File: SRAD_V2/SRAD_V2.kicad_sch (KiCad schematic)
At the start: 39 parts, among them SW1 SW_Push_Dual, SW2 SW_Nidec_CAS-120A1, U1 STM32F767ZIT6, U12 MAX-M10S, U13 MS5607-02BA, U14 MMC5983MA, U17 AS5F31G04SND-08LIN, U4 LSM6DSV80XTR

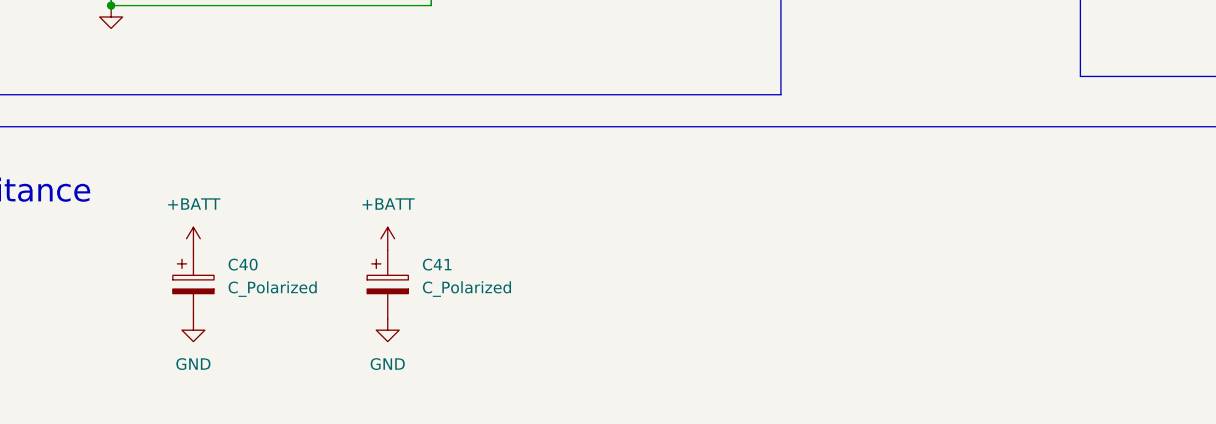
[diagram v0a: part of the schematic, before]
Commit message: Added an input LC filter
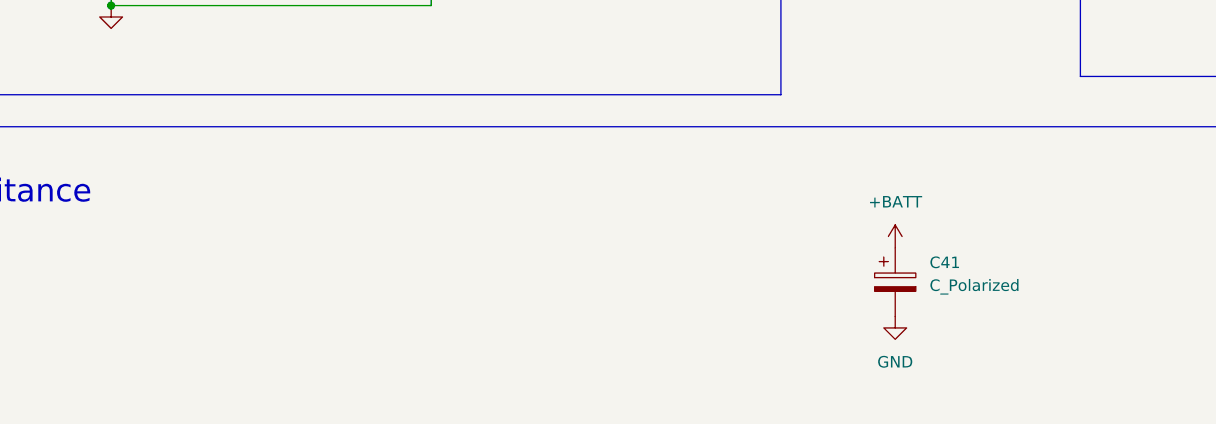
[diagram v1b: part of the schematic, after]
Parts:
- removed C40: C_Polarized, symbol Device:C_Polarized
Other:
- moved on the sheet: C41

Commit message: fiddling with the layout
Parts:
- removed SW1: SW_Push_Dual, Button_Switch_SMD:SW_DIP_SPSTx02_Slide_6.7x6.64mm_W6.73mm_P2.54mm_LowProfile_JPin, symbol Switch:SW_Push_Dual
- removed SW2: SW_Nidec_CAS-120A1, Button_Switch_SMD:Nidec_Copal_CAS-120A, symbol Switch:SW_Nidec_CAS-120A1
- added D1: WL-SMCW_1206, 150120SS75000:WL-SMCW_1206, symbol Red Led:WL-SMCW_1206
- added R13: 1k, symbol Device:R_Small
- added S1: TS18-5-15-SL-160-SMT-TR, push_button:SW_TS18-5-15-SL-160-SMT-TR, symbol push_button:TS18-5-15-SL-160-SMT-TR
- added S2: SLW-913535-2A-SMT, spdt_switch:SW_SLW-913535-2A-SMT, symbol spdt_switch:SLW-913535-2A-SMT
- FB1: footprint (none) -> Inductor_SMD:L_0603_1608Metric
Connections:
- net +3.3V: now also D1.2, S2.1, S2.4
- net GND: now also R13.2, S1.3, S1.4, S2.3, S2.6
- net at C39.2, U1.25 (NRST): now also S1.1, S1.2
- net at U1.138 (BOOT0): now also S2.2, S2.5
- new net: D1.1, R13.1
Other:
- note added: "LED indicator"
- note added: "approx 1.4mA of current"
- note added: "input capacitance"
- note removed: "Bulk Capacitance"
- moved on the sheet: C41

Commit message: more routing
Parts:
- R13: footprint (none) -> Resistor_SMD:R_0603_1608Metric
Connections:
- net +3.3V: now also C10.1, C11.1, C16.2, C17.2, C18.2, C20.2, C21.2, C22.2, C23.1, C24.2, U12.7 (VCC_IO), U12.8 (VCC), U13.1 (VDD), U14.13 (VDDIO), U14.2 (VDD), U17.8 (VCC), U4.5 (VDDIO), U4.8 (VDD)
- removed net +3V3: C10.1, C11.1, C16.2, C17.2, C18.2, C20.2, C21.2, C22.2, C23.1, C24.2, U12.6 (V_BCKP), U12.7 (VCC_IO), U12.8 (VCC), U13.1 (VDD), U14.13 (VDDIO), U14.2 (VDD), U17.8 (VCC), U4.5 (VDDIO), U4.8 (VDD)
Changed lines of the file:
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@@
 	)
 	(junction
-		(at 193.04 193.04)
-		(diameter 0)
-		(color 0 0 0 0)
-	)
-	(junction
 		(at 177.8 106.68)
 		(diameter 0)
@@
 	)
 	(junction
+		(at 191.77 193.04)
+		(diameter 0)
+		(color 0 0 0 0)
+	)
+	(junction
 		(at 95.25 44.45)
 		(diameter 0)
@@
 	)
 	(junction
-		(at 193.04 196.85)
-		(diameter 0)
-		(color 0 0 0 0)
-	)
-	(junction
 		(at 300.228 35.56)
 		(diameter 0)
@@
 	(wire
 		(pts
-			(xy 191.77 196.85) (xy 193.04 196.85)
-		)
-		(stroke
-			(width 0)
-			(type default)
-		)
-	)
-	(wire
-		(pts
 			(xy 168.91 106.68) (xy 168.91 110.49)
 		)
@@
 	(wire
 		(pts
-			(xy 193.04 193.04) (xy 193.04 196.85)
-		)
-		(stroke
-			(width 0)
-			(type default)
-		)
-	)
-	(wire
-		(pts
 			(xy 177.8 160.02) (xy 180.34 160.02)
 		)
@@
 	(wire
 		(pts
-			(xy 229.87 193.04) (xy 193.04 193.04)
-		)
-		(stroke
-			(width 0)
-			(type default)
-		)
-	)
-	(wire
-		(pts
 			(xy 92.71 81.28) (xy 95.25 81.28)
 		)
@@
 	(wire
 		(pts
-			(xy 193.04 196.85) (xy 194.31 196.85)
+			(xy 27.94 76.2) (xy 29.21 76.2)
 		)
 		(stroke
@@
 	(wire
 		(pts
-			(xy 27.94 76.2) (xy 29.21 76.2)
+			(xy 121.92 73.66) (xy 129.54 73.66)
 		)
 		(stroke
@@
 	(wire
 		(pts
-			(xy 121.92 73.66) (xy 129.54 73.66)
+			(xy 191.77 193.04) (xy 191.77 196.85)
 		)
 		(stroke
@@
 	(wire
 		(pts
+			(xy 191.77 193.04) (xy 229.87 193.04)
+		)
+		(stroke
+			(width 0)
+			(type default)
+		)
+	)
+	(wire
+		(pts
 			(xy 297.434 35.56) (xy 300.228 35.56)
 		)
@@
 	(wire
 		(pts
-			(xy 193.04 193.04) (xy 189.23 193.04)
+			(xy 189.23 193.04) (xy 191.77 193.04)
 		)
 		(stroke
@@
 		)
 	)
-	(global_label "+3V3"
+	(global_label "+3.3V"
 		(shape input)
 		(at 386.08 96.52 0)
@@
 		)
 	)
-	(global_label "+3V3"
+	(global_label "+3.3V"
 		(shape input)
 		(at 381 210.82 0)
@@
 		)
 	)
-	(global_label "+3V3"
+	(global_label "+3.3V"
 		(shape input)
 		(at 177.8 160.02 180)
@@
 		)
 	)
-	(global_label "+3V3"
+	(global_label "+3.3V"
 		(shape input)
 		(at 233.68 165.1 0)
@@
 		)
 	)
-	(global_label "+3V3"
+	(global_label "+3.3V"
 		(shape input)
 		(at 246.38 110.49 0)
@@
 		)
 	)
-	(global_label "+3V3"
+	(global_label "+3.3V"
 		(shape input)
 		(at 165.1 106.68 180)
@@
 		)
 	)
-	(global_label "+3V3"
+	(global_label "+3.3V"
 		(shape input)
 		(at 186.69 193.04 180)
@@
 			)
 		)
-		(property "Footprint" ""
+		(property "Footprint" "Resistor_SMD:R_0603_1608Metric"
 			(at 206.756 266.446 0)
 			(hide yes)

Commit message: more layout optimisation
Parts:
- removed C41: C_Polarized, symbol Device:C_Polarized
- added J1: Conn_01x04_Pin, Connector_PinHeader_2.54mm:PinHeader_1x04_P2.54mm_Vertical, symbol Connector:Conn_01x04_Pin
- added J7: 691210910002, Screw_Terminal:691210910002, symbol Screw Terminal:691210910002
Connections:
- net +3.3V: now also J1.3 (Pin_3)
- net EM_CH1: now also U1.91 (PG6); no longer U1.105 (PA13)
- net EM_CH2: now also U1.90 (PG5); no longer U1.104 (PA12)
- net EM_CH3: now also U1.89 (PG4); no longer U1.103 (PA11)
- net EM_CH4: now also U1.88 (PG3); no longer U1.102 (PA10)
- net GND: now also J1.4 (Pin_4), J7.2
- net Buzzer: now reaches BZ2.1 (+)
- net Buzzer: now also U1.70 (PB11)
- net SWCLK: now reaches U1.109 (PA14)
- net SWCLK: now also J1.2 (Pin_2)
- new net +7.4VBATT: J7.1
- new net SWDIO: J1.1 (Pin_1), U1.105 (PA13)
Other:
- note removed: "input capacitance"
- moved on the sheet: S2

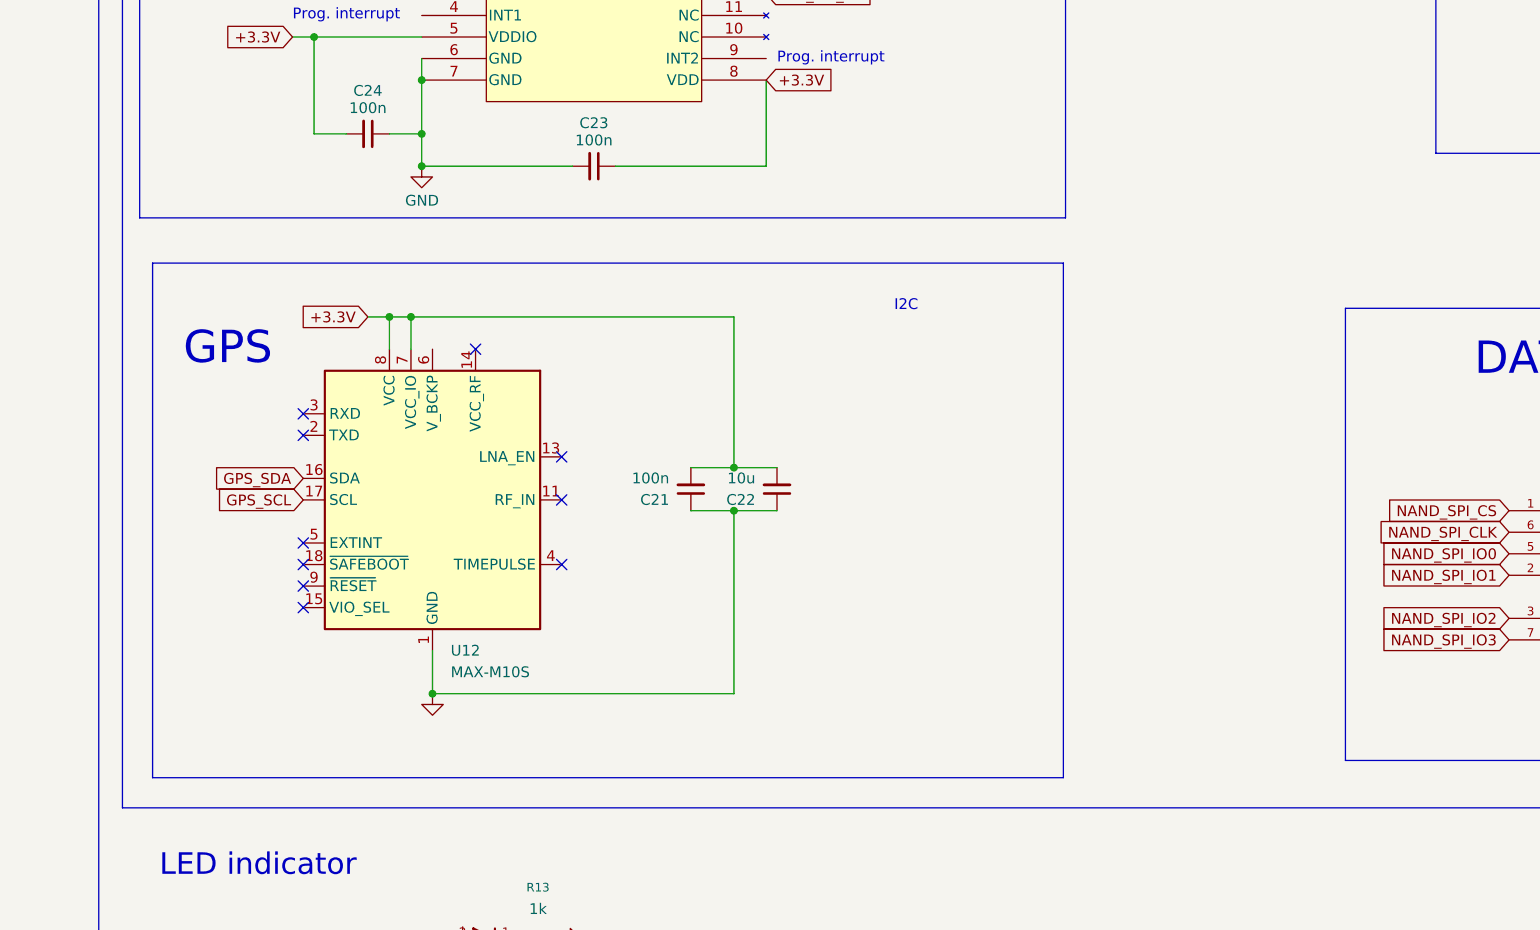
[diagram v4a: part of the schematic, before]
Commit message: Added important GPS circuitry
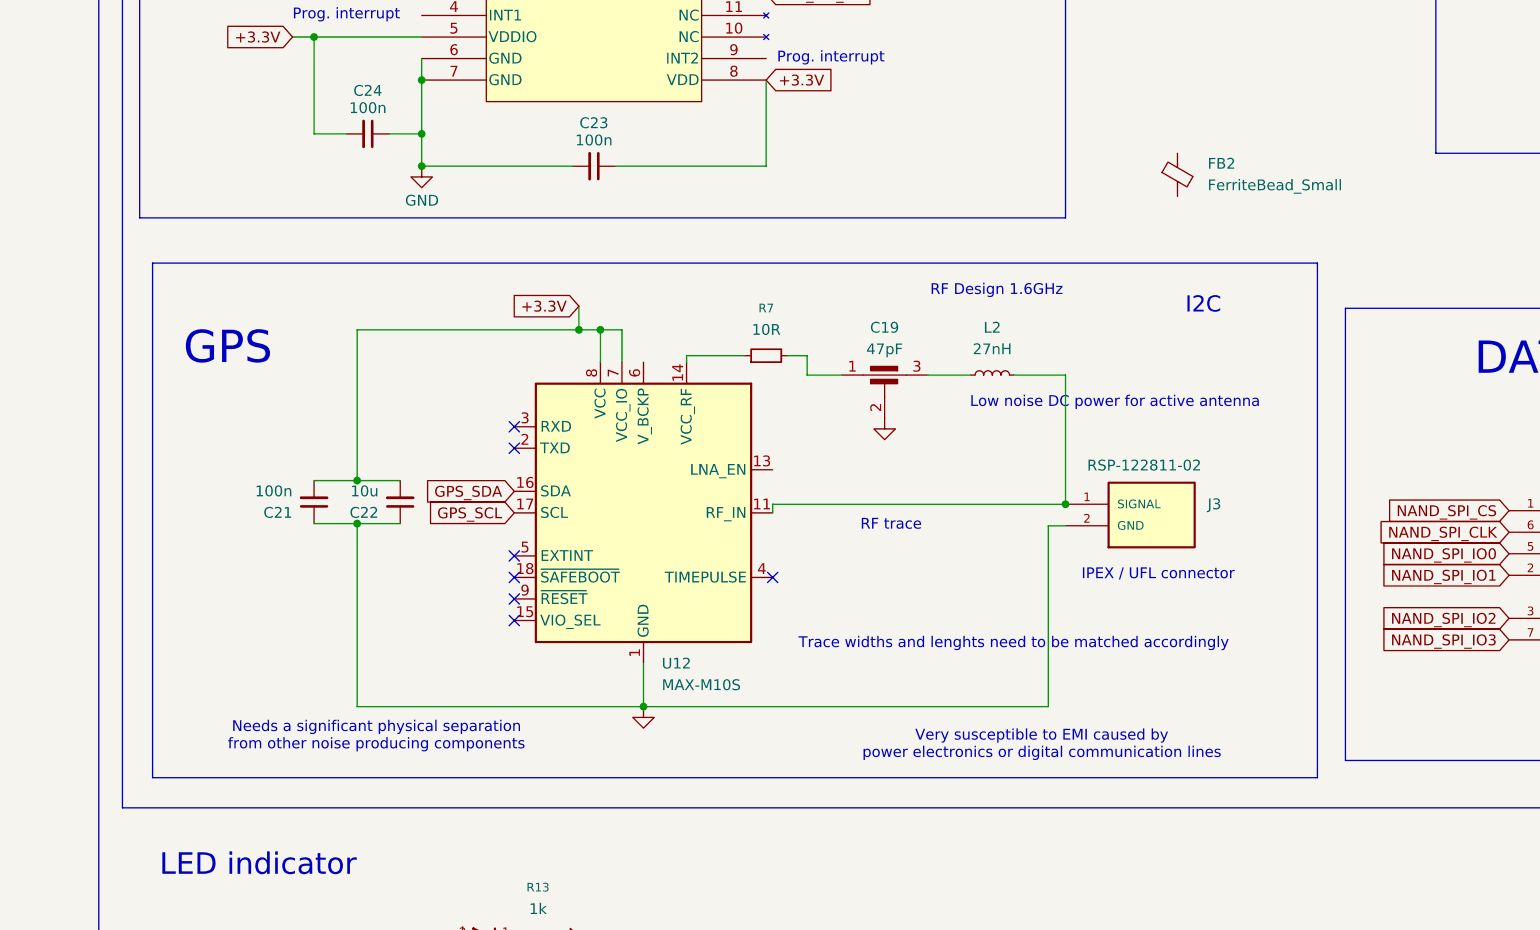
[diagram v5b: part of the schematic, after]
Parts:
- added C19: 47pF, symbol Device:C_Feedthrough
- added FB2: FerriteBead_Small, symbol Device:FerriteBead_Small
- added J3: RSP-122811-02, RSP_122811_02-2:SAMTEC_RSP-122811-02, symbol RSP-122811-02:RSP-122811-02
- added L2: 27nH, symbol Device:L_Small
- added R7: 10R, symbol Device:R_Small
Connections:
- net GND: now also C19.2, J3.2 (GND)
- net at U12.11 (RF_IN): now also J3.1 (SIGNAL), L2.2
- net at U12.14 (VCC_RF): now also R7.1
- new net: C19.3, L2.1
- new net: C19.1, R7.2
- no-connect marks 10 -> 7
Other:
- note added: "IPEX / UFL connector"
- note added: "Low noise DC power for active antenna"
- note added: "Needs a significant physical separation from other noise producing components"
- note added: "RF Design 1.6GHz"
- note added: "RF trace"
- note added: "Trace widths and lenghts need to be matched accordingly"
- note added: "Very susceptible to EMI caused by power electronics or digital communication lines"
- moved on the sheet: C21, C22, U12
